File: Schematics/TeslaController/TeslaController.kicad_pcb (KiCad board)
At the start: 2 copper layers, 71 x 95 mm, 100 parts, among them IC1 ATXMEGA256A3-A, P1 PWR_IN, P10 MicroSD, P11 KEYBOARD, P12 INVERTER, P13 DISPLAY, P14 INV_EN, P15 TEMP1, P16 TEMP2, P17 CURRENT_SENS, P2 PWR_OUT1, P3 ESP-12E, P4 ISP, P5 DEBUG, P6 BUZZER, P7 EXPANSION, P8 FAN1, P9 FAN2, Q1 BSS138, Q2 BSS138, Q3 BSS138, Q4 BSS138, Q5 BSS138, Q6 BSS138, Q7 BSS138, Q8 BSS138, Q9 BSS138, U1 AP1117, U2 AP1117D50, U3 AP1117D33, U4 TL431DBZ, Y1 DSX321SH

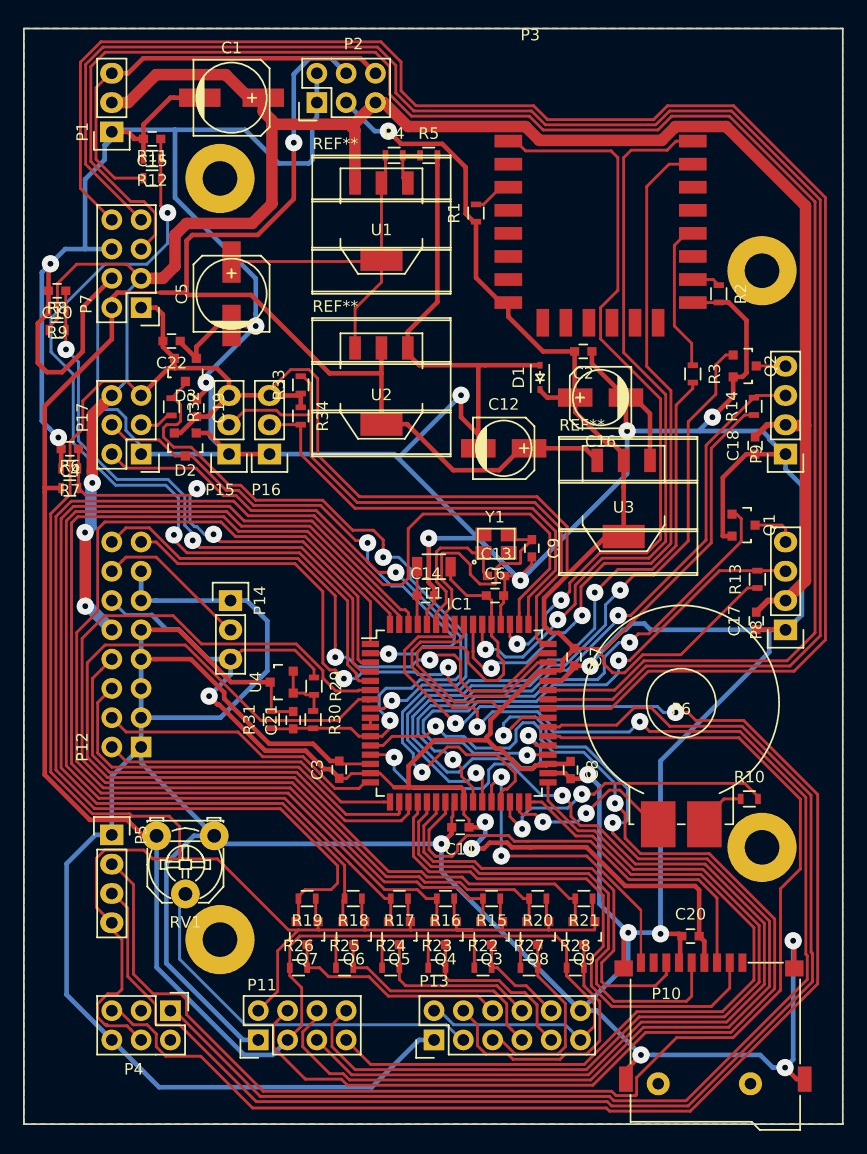
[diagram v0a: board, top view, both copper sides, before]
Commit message: Decided to send the controller PCB off to China rather than etching myself. So fixed up the silkscreen and reduced via sizes a bit.
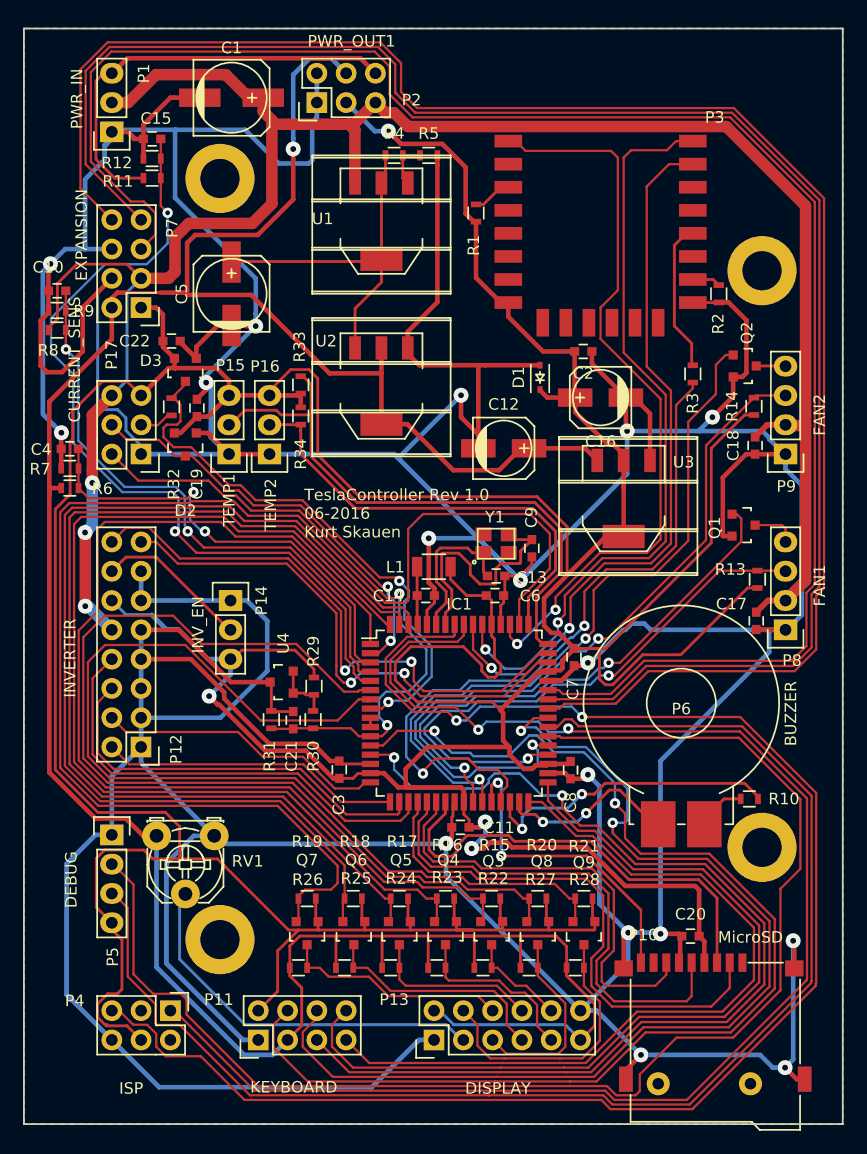
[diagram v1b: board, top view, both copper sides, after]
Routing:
- net ZERO_DETECT: track 46.6 -> 37.2 mm
- net CURSENS_L: track 54.7 -> 49.1 mm
- net KBD1: track 95.7 -> 90.2 mm
- net +3V3: track 497.1 -> 502.5 mm
- net CURSENS_N: track 62.1 -> 56.9 mm
- net FAN2_TACH: track 68.9 -> 65.8 mm
- net /PDI_CLK: track 135.6 -> 138.6 mm
- net WIFI_FLASH: track 65.3 -> 62.5 mm
- net /PDI_DATA: track 127.8 -> 129.7 mm
- net /ROT_ENC1: track 105.9 -> 104.1 mm
- net LCD_E: track 118.6 -> 120.4 mm
- net /EXP_MOSI: track 153.0 -> 151.4 mm
- net SENS_5V: track 41.2 -> 39.8 mm
- net /WIFI_RX: track 64.8 -> 66.2 mm
- net /ROT_ENC2: track 92.5 -> 91.1 mm
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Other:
- net class Default: trace_width 0.25 -> 0.2; via_dia 1.5 -> 0.9; via_drill 0.5 -> 0.4
- net class Power: via_dia 1.5 -> 1.3
- rule via_min_drill: 0.5 -> 0.4
- rule via_min_size: 1.5 -> 0.9
- board text added: "TeslaController Rev 1.0 06-2016 Kurt Skauen"

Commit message: - Changed the value of R30 & R31 to up the current sense reference voltage from 0.5V to 1.65V. - TeslaTuner now show current limits in Amps rather than a number between 0 and 4095.
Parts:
- R30: value 1k2 -> 470
- R31: value 300 -> 910
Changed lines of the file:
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@@
       (effects (font (size 1 1) (thickness 0.15)))
     )
-    (fp_text value 1k2 (at 0 1.9 270) (layer F.Fab) hide
+    (fp_text value 470 (at 0 1.9 270) (layer F.Fab) hide
       (effects (font (size 1 1) (thickness 0.15)))
     )
@@
       (effects (font (size 1 1) (thickness 0.15)))
     )
-    (fp_text value 300 (at 0 1.9 90) (layer F.Fab) hide
+    (fp_text value 910 (at 0 1.9 90) (layer F.Fab) hide
       (effects (font (size 1 1) (thickness 0.15)))
     )
